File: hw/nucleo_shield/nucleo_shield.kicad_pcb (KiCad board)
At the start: 2 copper layers, 150.1 x 90.2 mm, 71 parts, among them CN101 Nucleo-F411RE-CN10, CN71 Nucleo-F411RE-CN7, P1 CONN_INH1, P10 CONN_OUTH1, P11 CONN_OUTH2, P12 CONN_RS485_OUT, P13 CONN_RS485_IN, P14 CONN_OUT2, P15 CONN_ANALOG, P16 CONN_EXTI2C, P17 CONN_EXT, P2 CONN_OUT3, P3 CONN_OUT1, P4 POWER_CON, P5 CONN_INH2, P6 ETH_CONN, P7 CONN_LCD_SD, P8 CONN_OUT4, P9 CONN_SCT, U1 74HC595, U10 ULN2803, U11 74HC595, U12 74HC595, U2 74HC595, U3 LTV-847, U4 LTV-847, U5 LTV-847, U6 LTV-847, U7 PCF8574A, U8 PCF8574A, U9 ULN2803

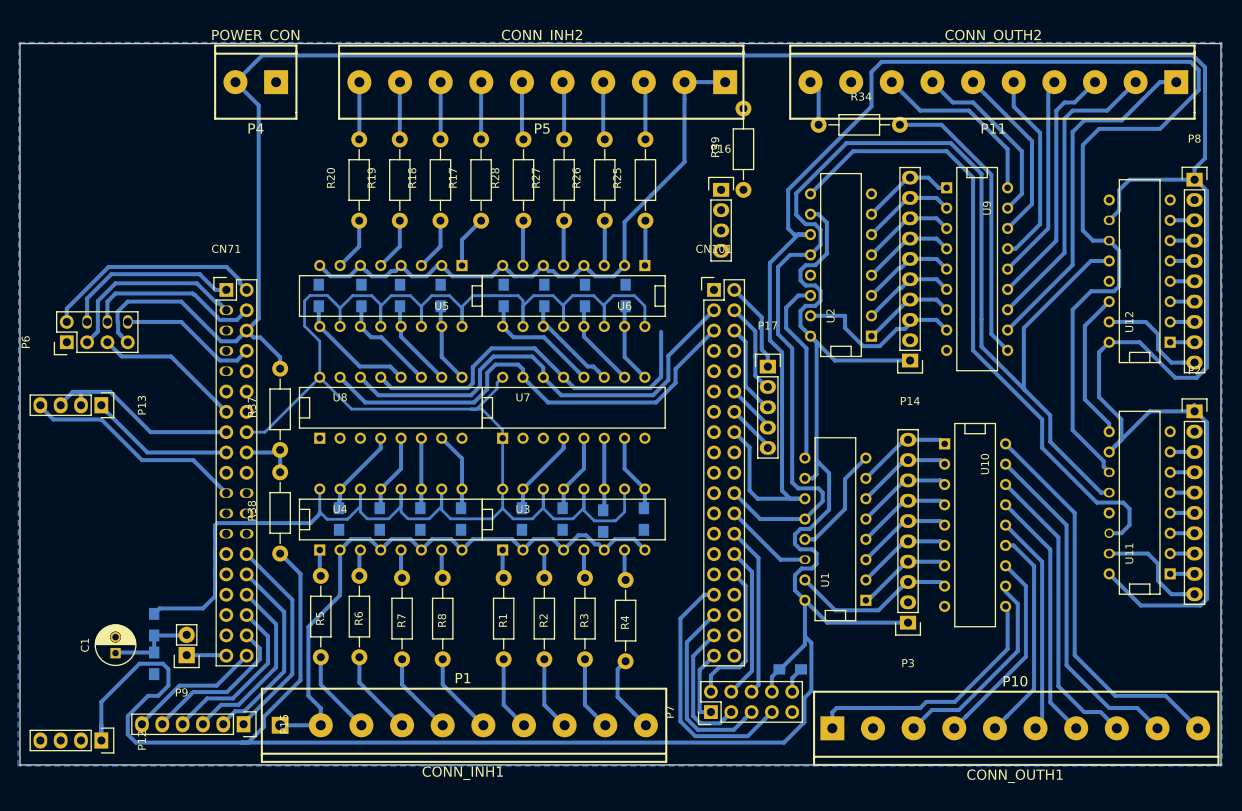
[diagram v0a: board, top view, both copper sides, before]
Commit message: Add one wire, expander, etc
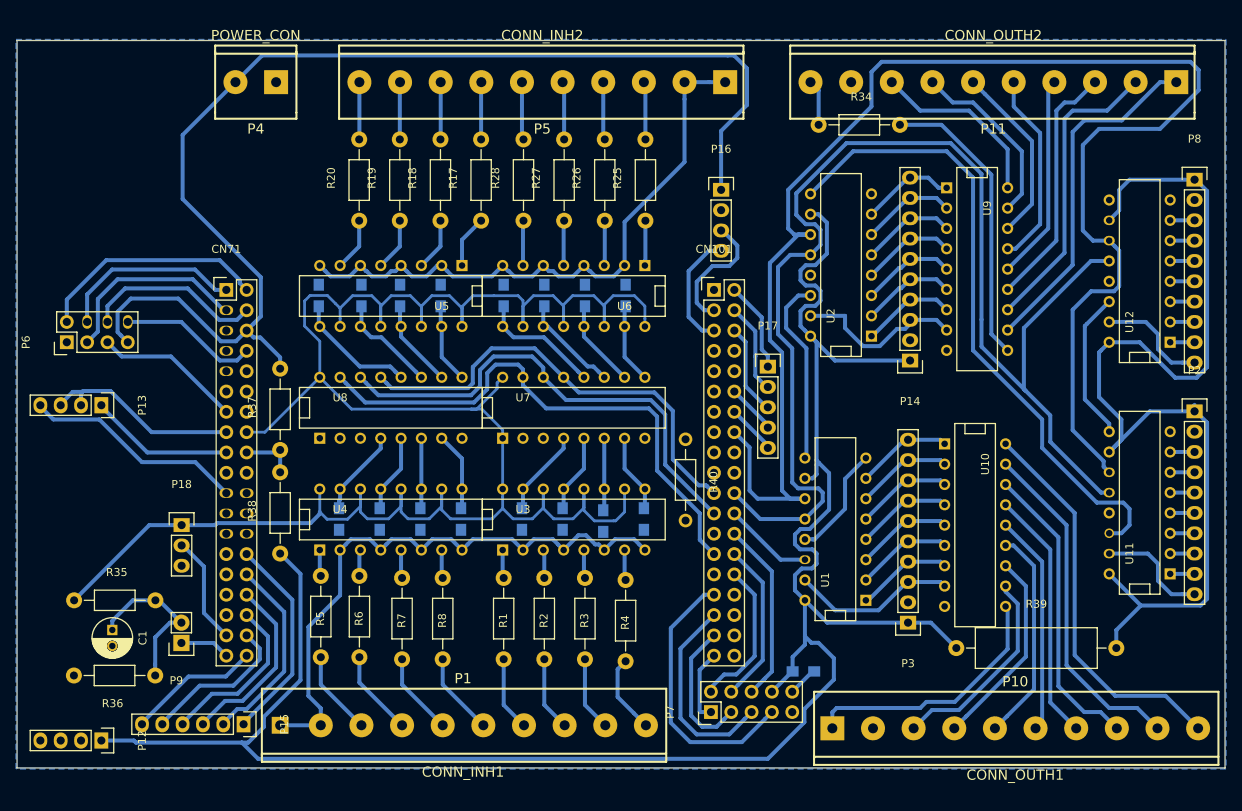
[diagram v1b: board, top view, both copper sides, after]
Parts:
- added P18: CONN_1WIRE, Pin_Headers:Pin_Header_Straight_1x03, F.Cu at (115.7, 118.6)
- added R40: R, Resistors_ThroughHole:Resistor_Horizontal_RM10mm, F.Cu at (178.7, 107.9)
- R35, R36: footprint Resistors_SMD:R_0805_HandSoldering -> Resistors_ThroughHole:Resistor_Horizontal_RM10mm; moved to F.Cu
- R39: footprint Resistors_ThroughHole:Resistor_Horizontal_RM10mm -> Resistors_ThroughHole:Resistor_Horizontal_RM20mm
- moved R39 67.8 mm to (212.5, 134.0), turned to 0 degrees
- moved R35 10.5 mm to (102.3, 128.0), turned to 0 degrees
- moved C1 2.92 mm to (107.0, 131.7), turned to 270 degrees
- moved R33 1.67 mm to (193.4, 136.9)
- moved P9 1.66 mm to (115.7, 133.3)
- moved R36 1.53 mm to (112.4, 137.4), turned to 180 degrees
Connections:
- CN101 pad 1: IO_INT -> (no net)
- CN101 pad 21: (no net) -> IO_INT
- CN101 pad 23: (no net) -> I2C3_SCL
- CN101 pad 27: (no net) -> I2C3_SDA
- CN71 pad 35: (no net) -> 1WIRE_IN
- U7 pad 14: I2C1_SCL -> I2C3_SCL
- U7 pad 15: I2C1_SDA -> I2C3_SDA
- U8 pad 14: I2C1_SCL -> I2C3_SCL
- U8 pad 15: I2C1_SDA -> I2C3_SDA
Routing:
- net I2C3_SDA: track 0.00 -> 68.1 mm
- net I2C3_SCL: track 0.00 -> 60.8 mm
- net +5V: track 591.6 -> 535.2 mm
- net I2C1_SDA: track 58.5 -> 14.7 mm
- net I2C1_SCL: track 57.6 -> 16.2 mm
- net 1WIRE_IN: track 0.00 -> 13.6 mm
- net Net-(C1-Pad1): track 11.1 -> 20.8 mm
- net IO_INT: track 47.1 -> 56.5 mm
- net +3V3: track 257.8 -> 262.0 mm
- net SD_CS: track 31.7 -> 34.2 mm
- net LCD_DC: track 24.0 -> 25.5 mm
- net SPI1_MOSI: track 21.4 -> 22.7 mm
- net SCT_IN: track 4.98 -> 6.36 mm
- net SPI3_MISO: track 27.7 -> 29.1 mm
- net SPI1_MISO: track 19.2 -> 20.3 mm
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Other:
- board size 150.1 x 90.2 mm -> 151 x 90.9 mm

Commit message: Nucleo shield: mino modifications
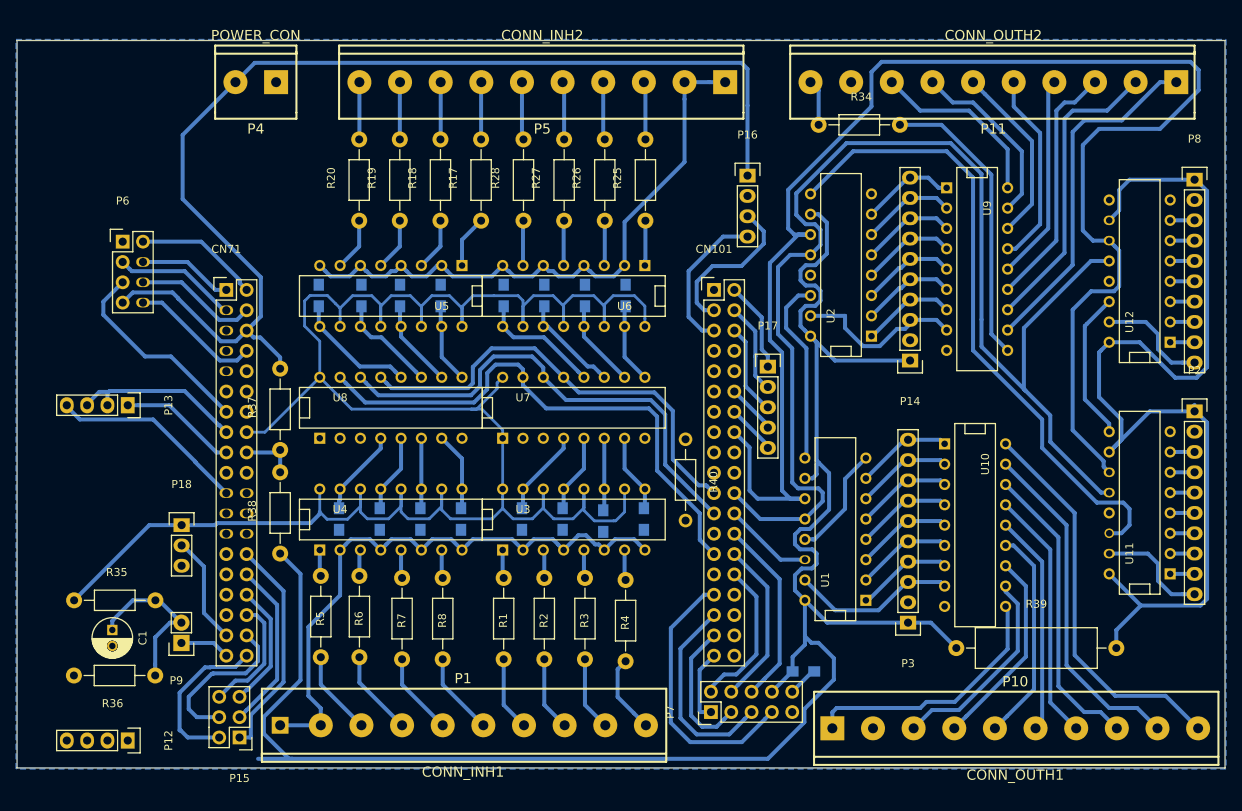
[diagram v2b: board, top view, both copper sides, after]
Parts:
- P15: value CONN_ANALOG -> CONN_EXT2; footprint Pin_Headers:Pin_Header_Straight_1x06 -> Pin_Headers:Pin_Header_Straight_2x03
- moved P6 14.4 mm to (108.3, 83.2), turned to 0 degrees
- moved P16 3.75 mm to (186.4, 74.9)
- moved P12 3.30 mm to (109.0, 145.5)
- moved P13 3.30 mm to (109.0, 103.6)
- moved P15 1.73 mm to (122.9, 145.2), turned to 180 degrees
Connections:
- P15 pad 2: Net-(CN71-Pad30) -> Net-(CN71-Pad38)
- P15 pad 3: Net-(CN71-Pad32) -> Net-(CN71-Pad30)
- P15 pad 4: Net-(CN71-Pad34) -> Net-(CN71-Pad36)
- P15 pad 5: Net-(CN71-Pad36) -> Net-(CN71-Pad32)
- P15 pad 6: Net-(CN71-Pad38) -> Net-(CN71-Pad34)
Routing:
- net +5V: track 535.2 -> 508.2 mm
- net SPI3_MISO: track 29.1 -> 15.7 mm
- net SPI3_SCK: track 23.2 -> 11.9 mm
- net SPI3_MOSI: track 24.7 -> 15.5 mm
- net Net-(CN71-Pad32): track 22.8 -> 15.7 mm
- net ETH_RST: track 22.4 -> 15.4 mm
- net ETH_CS: track 18.5 -> 25.5 mm
- net Net-(CN71-Pad34): track 21.1 -> 15.1 mm
- net I2C1_SDA: track 14.7 -> 18.8 mm
- net I2C1_SCL: track 16.2 -> 20.2 mm
- net Net-(CN71-Pad38): track 16.7 -> 20.3 mm
- net RS_DE: track 25.4 -> 22.1 mm
- net RS_TX: track 27.9 -> 24.6 mm
- net RS_RX: track 18.5 -> 15.2 mm
- net Net-(CN71-Pad30): track 24.5 -> 21.4 mm
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
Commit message: Nucleo: add more extension header for SPI, etc
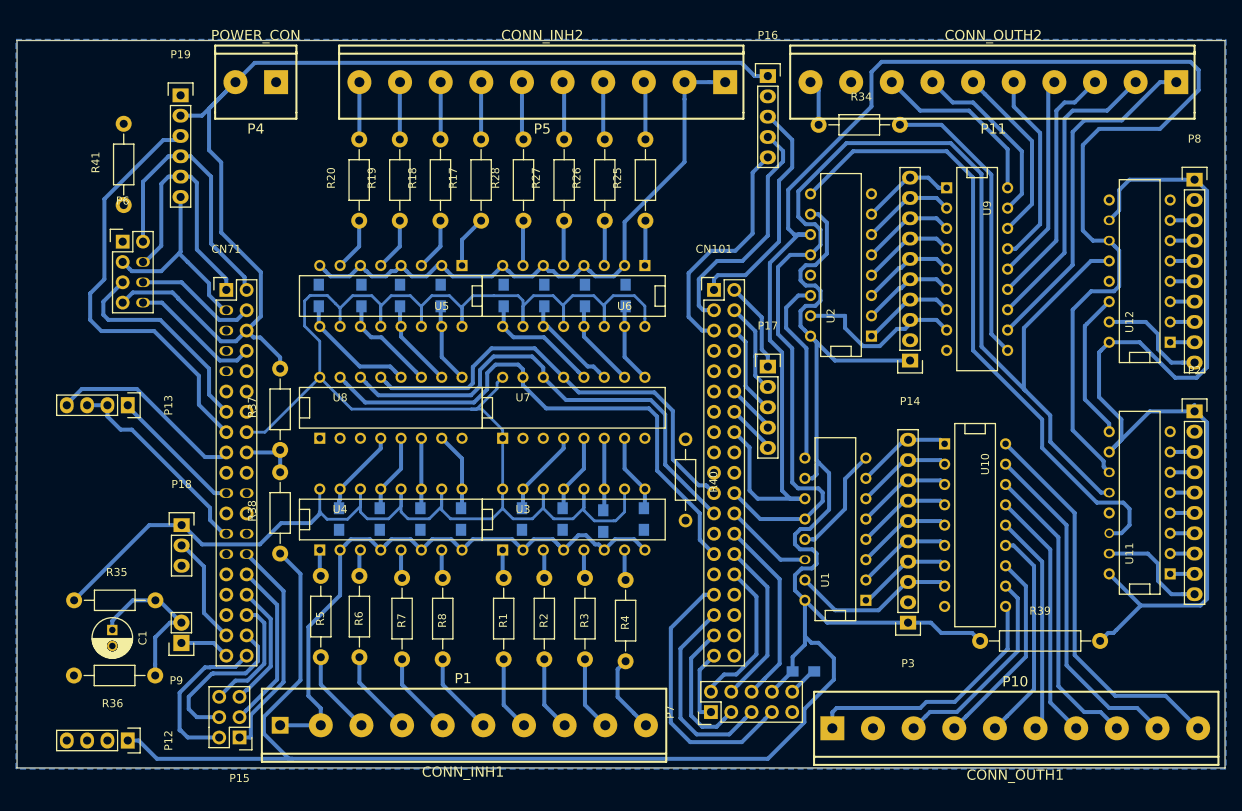
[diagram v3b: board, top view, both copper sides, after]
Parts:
- added P19: CONN_EXT_SPI, Pin_Headers:Pin_Header_Straight_1x06, F.Cu at (115.6, 64.9)
- added R41: R, Resistors_ThroughHole:Resistor_Horizontal_RM10mm, F.Cu at (108.5, 73.5)
- P16: footprint Pin_Headers:Pin_Header_Straight_1x04 -> Pin_Headers:Pin_Header_Straight_1x05
- R39: footprint Resistors_ThroughHole:Resistor_Horizontal_RM20mm -> Resistors_ThroughHole:Resistor_Horizontal_RM15mm
- moved P16 12.7 mm to (189.0, 62.5)
- moved R39 10.5 mm to (223.0, 133.1)
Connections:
- CN101 pad 1: (no net) -> I2C_GPIO
- CN71 pad 15: RS_DE -> EXT_SPI_SS
- CN71 pad 17: RS_RX -> RS_TX
- CN71 pad 21: RS_TX -> RS_RX
- CN71 pad 25: (no net) -> RS_DE
- P16 pad 3: I2C1_SCL -> I2C_GPIO
- P16 pad 4: I2C1_SDA -> I2C1_SCL
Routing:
- net EXT_SPI_SS: track 0.00 -> 53.6 mm
- net I2C_GPIO: track 0.00 -> 29.1 mm
- net SPI3_SCK: track 11.9 -> 30.9 mm
- net SPI3_MISO: track 15.7 -> 34.4 mm
- net +5V: track 508.2 -> 523.8 mm
- net I2C1_SDA: track 18.8 -> 29.7 mm
- net I2C1_SCL: track 20.2 -> 30.7 mm
- net SPI3_MOSI: track 15.5 -> 25.7 mm
- net RS_DE: track 22.1 -> 26.1 mm
- net ETH_CS: track 25.5 -> 27.4 mm
- net +3V3: track 262.0 -> 263.9 mm
- net RS_RX: track 15.2 -> 17.0 mm

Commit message: Nucleo: minor fixup to PCB (track spacing)
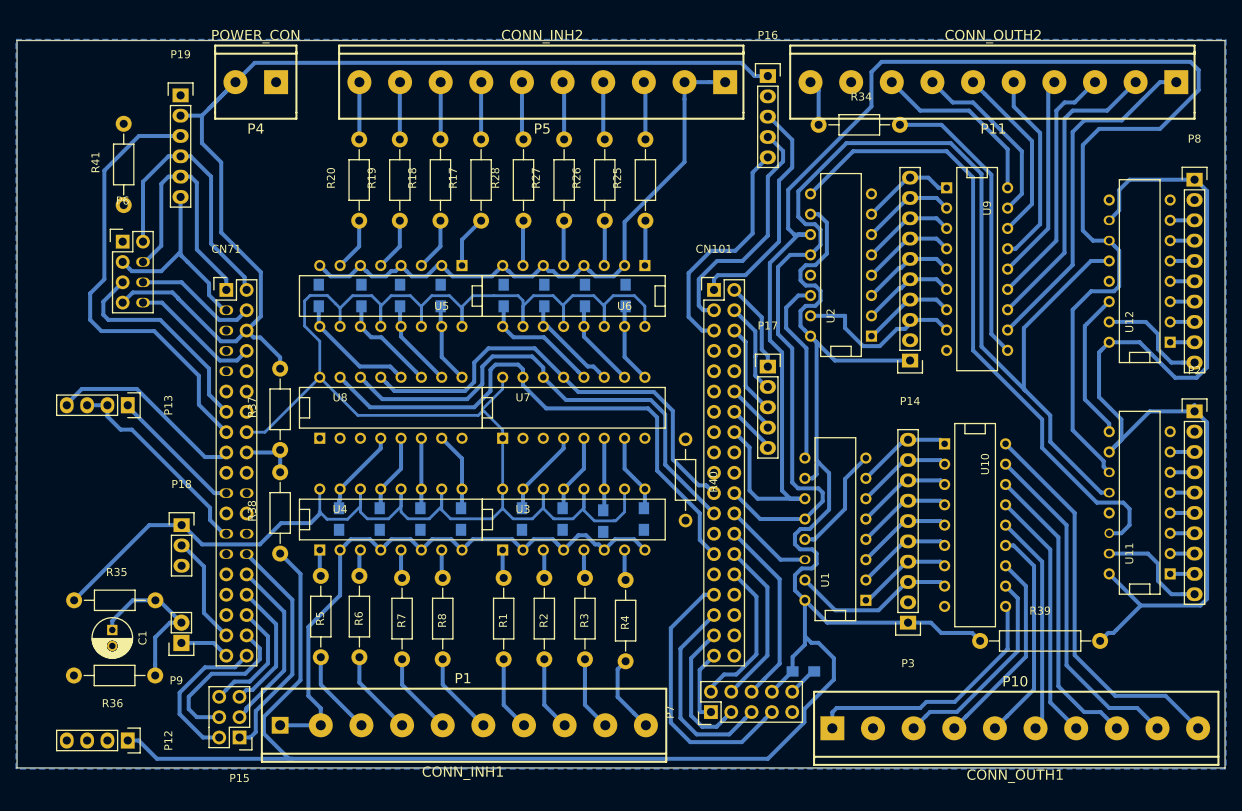
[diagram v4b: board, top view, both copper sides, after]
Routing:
- net EXT_SPI_SS: track 53.6 -> 55.8 mm
- net Net-(CN71-Pad38): track 20.3 -> 19.1 mm
- net Net-(CN71-Pad32): track 15.7 -> 16.6 mm
- net Net-(CN71-Pad28): track 27.9 -> 28.8 mm
- net I2C3_SDA: track 68.1 -> 68.9 mm
- net Net-(CN71-Pad30): track 21.4 -> 22.1 mm
- net IO_INT: track 56.5 -> 57.0 mm
- net +5V: track 523.8 -> 523.3 mm

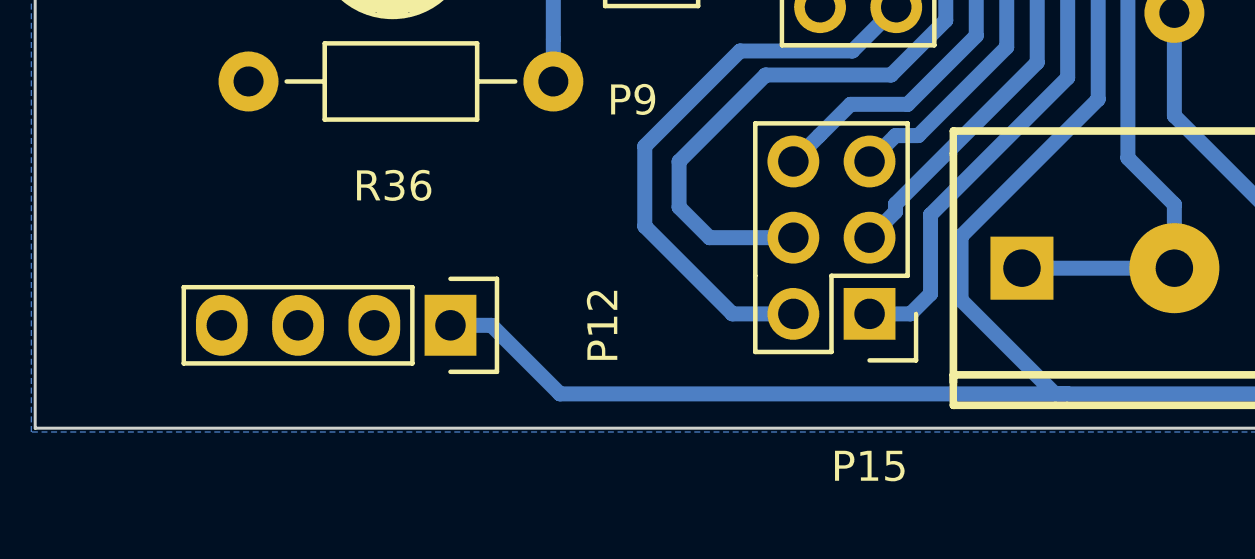
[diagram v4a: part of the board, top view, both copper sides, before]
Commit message: Nucleo: fix RS485 module spacing
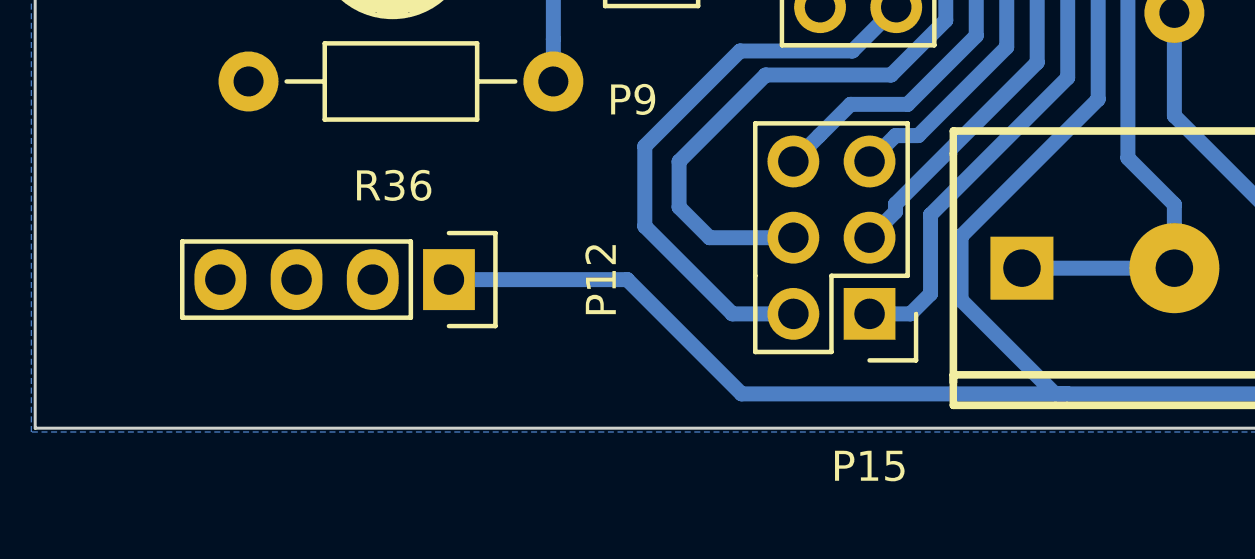
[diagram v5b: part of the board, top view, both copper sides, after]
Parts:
- moved P12 1.52 mm to (108.9, 144.0)
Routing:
- net +5V: track 523.3 -> 524.0 mm
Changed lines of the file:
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@@
-(kicad_pcb (version 4) (host pcbnew "(after 2015-mar-04 BZR unknown)-product")
+(kicad_pcb (version 4) (host pcbnew "(2016-05-03 BZR 6770, Git 22c4e4d)-product")
   (general
     (links 315)
-    (no_connects 10)
-    (area 95.072999 57.988999 246.176001 149.021001)
+    (no_connects 11)
+    (area 93.24879 55.93052 247.048143 158.955001)
     (thickness 1.6)
     (drawings 6)
@@
       (hpglpenspeed 20)
       (hpglpendiameter 15)
-      (hpglpenoverlay 2)
       (psnegative false)
       (psa4output false)
@@
   )
   (module Pin_Headers:Pin_Header_Straight_1x04 (layer F.Cu)
-    (at 108.966 145.542 270)
+    (at 108.9152 144.018 270)
     (descr "Through hole pin header")
     (tags "pin header")
@@
   (segment (start 128.143 118.364) (end 125.476 121.031) (width 0.5) (layer B.Cu) (net 47))
   (segment (start 132.969 116.967) (end 132.969 117.221) (width 0.5) (layer B.Cu) (net 47))
+  (segment (start 129.54 147.828) (end 118.6688 147.828) (width 0.5) (layer B.Cu) (net 48))
+  (segment (start 118.6688 147.828) (end 114.8588 144.018) (width 0.5) (layer B.Cu) (net 48))
+  (segment (start 114.8588 144.018) (end 108.9152 144.018) (width 0.5) (layer B.Cu) (net 48))
   (segment (start 118.237 67.437) (end 118.237 70.866) (width 0.5) (layer B.Cu) (net 48))
   (segment (start 118.237 70.866) (end 120.65 73.279) (width 0.5) (layer B.Cu) (net 48))
@@
   (segment (start 125.603 92.5195) (end 124.688599 93.433901) (width 0.5) (layer B.Cu) (net 48))
   (segment (start 124.688599 93.433901) (end 123.825 94.2975) (width 0.5) (layer B.Cu) (net 48))
-  (segment (start 129.54 147.828) (end 112.6156 147.828) (width 0.5) (layer B.Cu) (net 48))
-  (segment (start 112.6156 147.828) (end 110.3296 145.542) (width 0.5) (layer B.Cu) (net 48))
-  (segment (start 110.3296 145.542) (end 108.966 145.542) (width 0.5) (layer B.Cu) (net 48))
   (segment (start 215.512 133.096) (end 214.512511 132.096511) (width 0.5) (layer B.Cu) (net 48))
   (segment (start 214.512511 132.096511) (end 210.646011 132.096511) (width 0.5) (layer B.Cu) (net 48))
